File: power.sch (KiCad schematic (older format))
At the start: 50 parts, among them J10 Barrel_Jack_Switch, U6 ISL8033A, U7 TPS74401_VQFN, U8 LTC3633

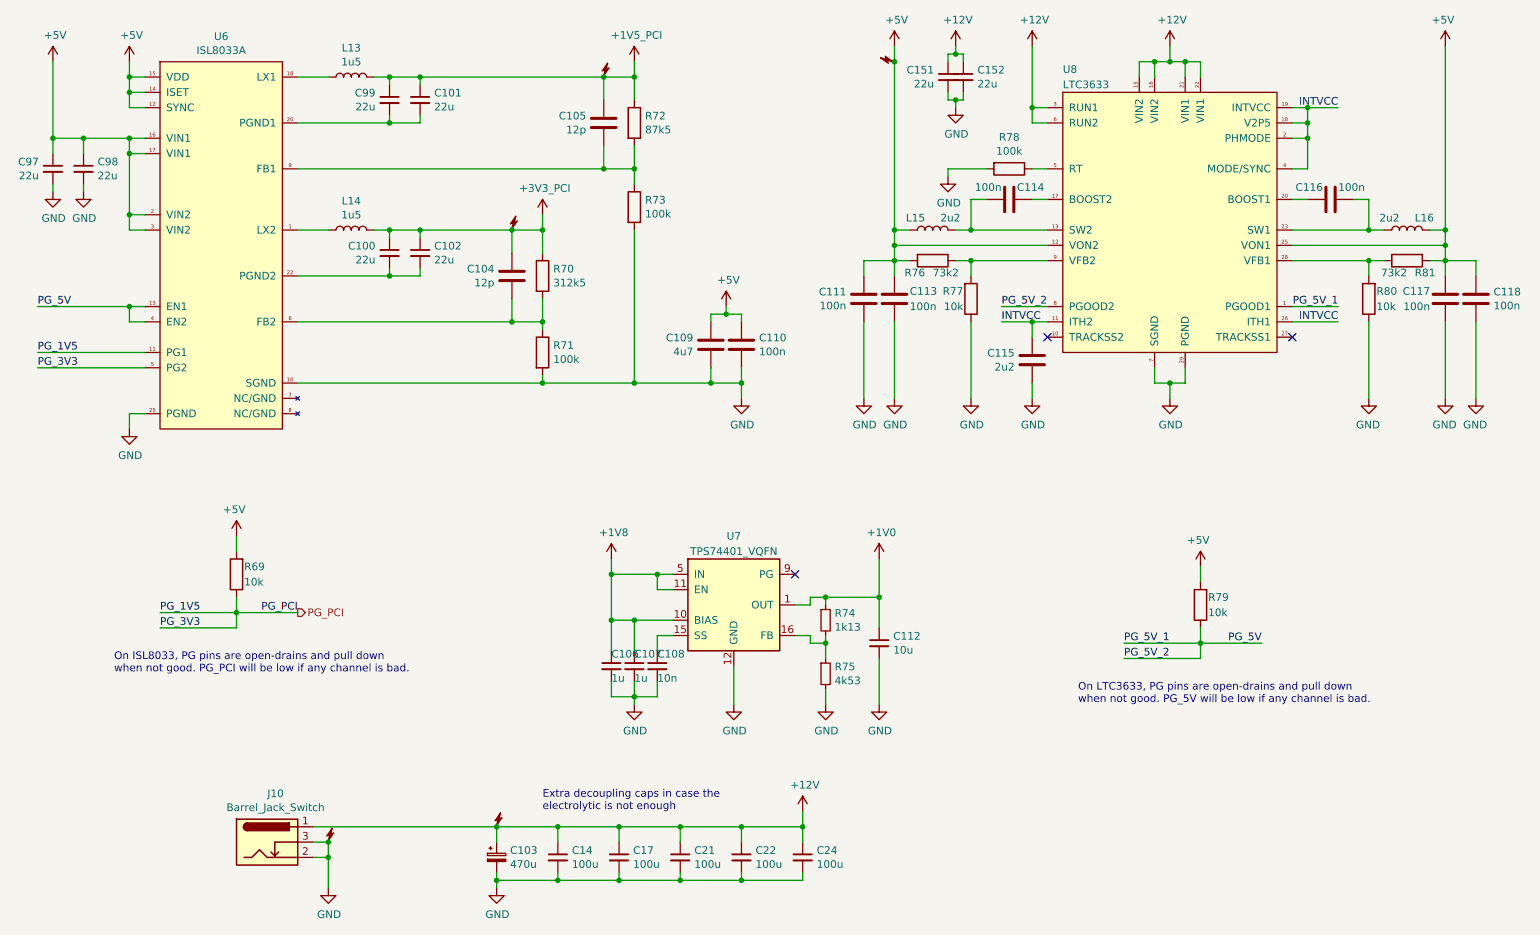
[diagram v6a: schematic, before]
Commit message: sch, pcb: Add testpads on lots of signals
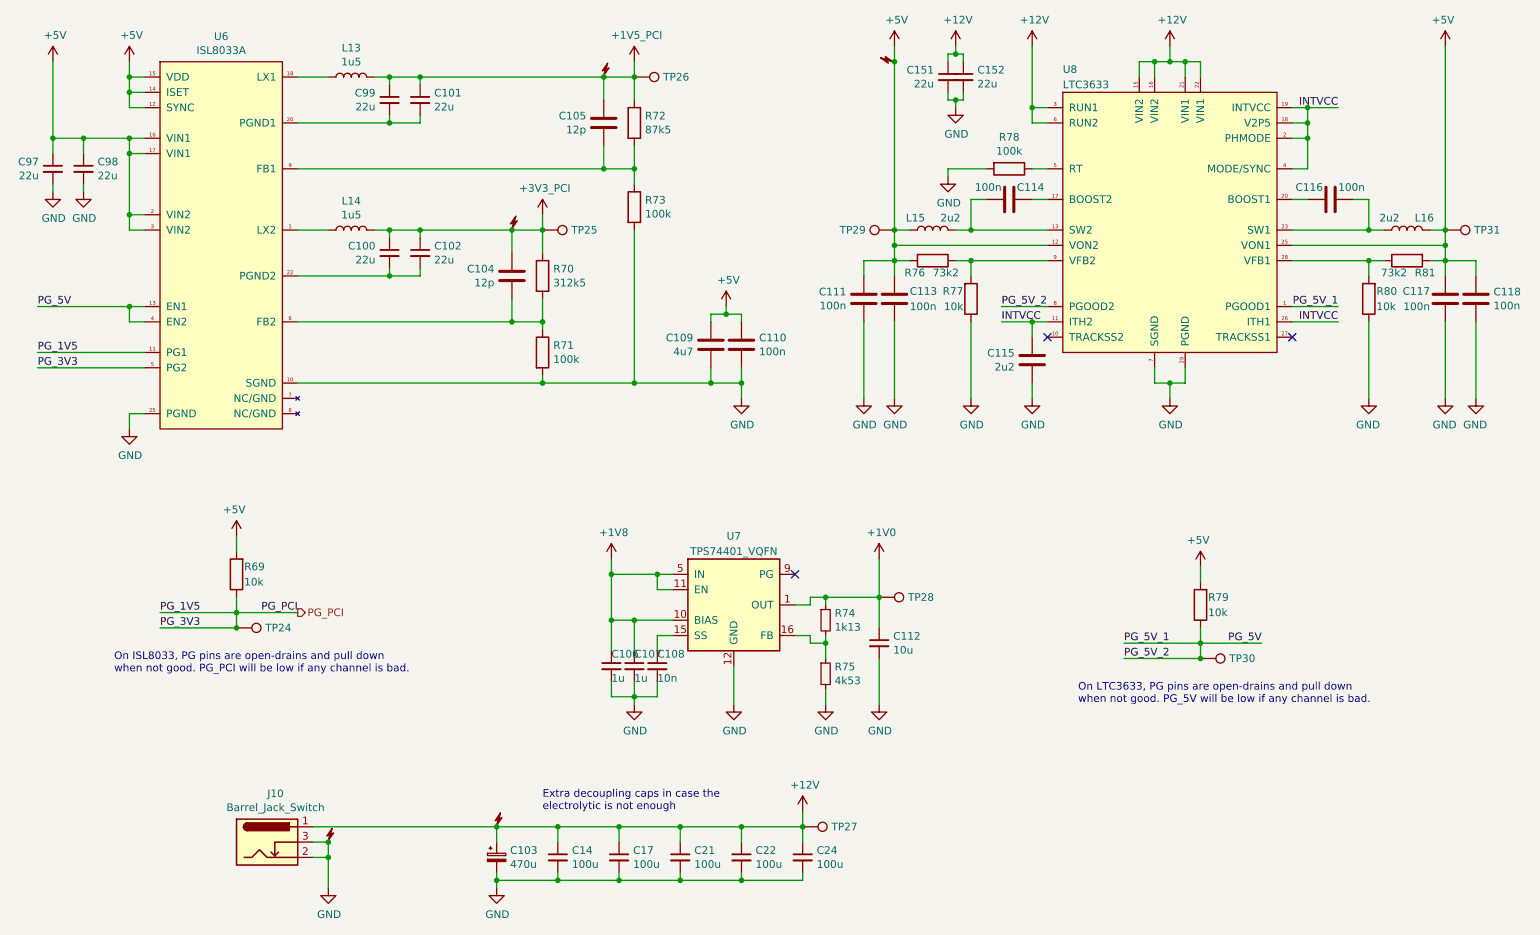
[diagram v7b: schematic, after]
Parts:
- added TP24, TP25, TP26, TP27, TP28, TP29, TP30, TP31: TestPoint, TestPoint:TestPoint_Pad_D1.0mm, symbol Connector:TestPoint
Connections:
- net +12V: now also TP27.1
- net +1V0: now also TP28.1
- net +1V5_PCI: now also TP26.1
- net +3V3_PCI: now also TP25.1
- net +5V: now also TP29.1, TP31.1
- net PG_5V: now also TP30.1
- net PG_PCI: now also TP24.1
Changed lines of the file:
@@
 Wire Wire Line
 	3000 6700 4200 6700
+$Comp
+L Connector:TestPoint TP?
+U 1 1 5D4E5684
+P 2500 5400
+AR Path="/5D05A5E1/5D4E5684" Ref="TP?"  Part="1"
+AR Path="/5CE77C37/5D4E5684" Ref="TP?"  Part="1"
+AR Path="/5D0C4621/5D4E5684" Ref="TP24"  Part="1"
+F 0 "TP24" V 2500 5588 50  0000 L CNN
+F 1 "TestPoint" V 2545 5588 50  0001 L CNN
+F 2 "TestPoint:TestPoint_Pad_D1.0mm" H 2700 5400 50  0001 C CNN
+F 3 "~" H 2700 5400 50  0001 C CNN
+	1    2500 5400
+	0    1    1    0
+$EndComp
+Connection ~ 2500 5400
+$Comp
+L Connector:TestPoint TP?
+U 1 1 5D514751
+P 8800 5600
+AR Path="/5D05A5E1/5D514751" Ref="TP?"  Part="1"
+AR Path="/5CE77C37/5D514751" Ref="TP?"  Part="1"
+AR Path="/5D0C4621/5D514751" Ref="TP30"  Part="1"
+F 0 "TP30" V 8800 5788 50  0000 L CNN
+F 1 "TestPoint" V 8845 5788 50  0001 L CNN
+F 2 "TestPoint:TestPoint_Pad_D1.0mm" H 9000 5600 50  0001 C CNN
+F 3 "~" H 9000 5600 50  0001 C CNN
+	1    8800 5600
+	0    1    1    0
+$EndComp
+Connection ~ 8800 5600
+$Comp
+L Connector:TestPoint TP?
+U 1 1 5D515165
+P 5100 1800
+AR Path="/5D05A5E1/5D515165" Ref="TP?"  Part="1"
+AR Path="/5CE77C37/5D515165" Ref="TP?"  Part="1"
+AR Path="/5D0C4621/5D515165" Ref="TP26"  Part="1"
+F 0 "TP26" V 5100 1988 50  0000 L CNN
+F 1 "TestPoint" V 5145 1988 50  0001 L CNN
+F 2 "TestPoint:TestPoint_Pad_D1.0mm" H 5300 1800 50  0001 C CNN
+F 3 "~" H 5300 1800 50  0001 C CNN
+	1    5100 1800
+	0    1    1    0
+$EndComp
+$Comp
+L Connector:TestPoint TP?
+U 1 1 5D51627F
+P 4500 2800
+AR Path="/5D05A5E1/5D51627F" Ref="TP?"  Part="1"
+AR Path="/5CE77C37/5D51627F" Ref="TP?"  Part="1"
+AR Path="/5D0C4621/5D51627F" Ref="TP25"  Part="1"
+F 0 "TP25" V 4500 2988 50  0000 L CNN
+F 1 "TestPoint" V 4545 2988 50  0001 L CNN
+F 2 "TestPoint:TestPoint_Pad_D1.0mm" H 4700 2800 50  0001 C CNN
+F 3 "~" H 4700 2800 50  0001 C CNN
+	1    4500 2800
+	0    1    1    0
+$EndComp
+$Comp
+L Connector:TestPoint TP?
+U 1 1 5D5167E4
+P 10400 2800
+AR Path="/5D05A5E1/5D5167E4" Ref="TP?"  Part="1"
+AR Path="/5CE77C37/5D5167E4" Ref="TP?"  Part="1"
+AR Path="/5D0C4621/5D5167E4" Ref="TP31"  Part="1"
+F 0 "TP31" V 10400 2988 50  0000 L CNN
+F 1 "TestPoint" V 10445 2988 50  0001 L CNN
+F 2 "TestPoint:TestPoint_Pad_D1.0mm" H 10600 2800 50  0001 C CNN
+F 3 "~" H 10600 2800 50  0001 C CNN
+	1    10400 2800
+	0    1    1    0
+$EndComp
+$Comp
+L Connector:TestPoint TP?
+U 1 1 5D5189F8
+P 6800 2800
+AR Path="/5D05A5E1/5D5189F8" Ref="TP?"  Part="1"
+AR Path="/5CE77C37/5D5189F8" Ref="TP?"  Part="1"
+AR Path="/5D0C4621/5D5189F8" Ref="TP29"  Part="1"
+F 0 "TP29" V 6800 2988 50  0000 L CNN
+F 1 "TestPoint" V 6845 2988 50  0001 L CNN
+F 2 "TestPoint:TestPoint_Pad_D1.0mm" H 7000 2800 50  0001 C CNN
+F 3 "~" H 7000 2800 50  0001 C CNN
+	1    6800 2800
+	0    -1   -1   0
+$EndComp
+$Comp
+L Connector:TestPoint TP?
+U 1 1 5D51982C
+P 6700 5200
+AR Path="/5D05A5E1/5D51982C" Ref="TP?"  Part="1"
+AR Path="/5CE77C37/5D51982C" Ref="TP?"  Part="1"
+AR Path="/5D0C4621/5D51982C" Ref="TP28"  Part="1"
+F 0 "TP28" V 6700 5388 50  0000 L CNN
+F 1 "TestPoint" V 6745 5388 50  0001 L CNN
+F 2 "TestPoint:TestPoint_Pad_D1.0mm" H 6900 5200 50  0001 C CNN
+F 3 "~" H 6900 5200 50  0001 C CNN
+	1    6700 5200
+	0    1    1    0
+$EndComp
+$Comp
+L Connector:TestPoint TP?
+U 1 1 5D51A38B
+P 6200 6700
+AR Path="/5D05A5E1/5D51A38B" Ref="TP?"  Part="1"
+AR Path="/5CE77C37/5D51A38B" Ref="TP?"  Part="1"
+AR Path="/5D0C4621/5D51A38B" Ref="TP27"  Part="1"
+F 0 "TP27" V 6200 6888 50  0000 L CNN
+F 1 "TestPoint" V 6245 6888 50  0001 L CNN
+F 2 "TestPoint:TestPoint_Pad_D1.0mm" H 6400 6700 50  0001 C CNN
+F 3 "~" H 6400 6700 50  0001 C CNN
+	1    6200 6700
+	0    1    1    0
+$EndComp
 $EndSCHEMATC

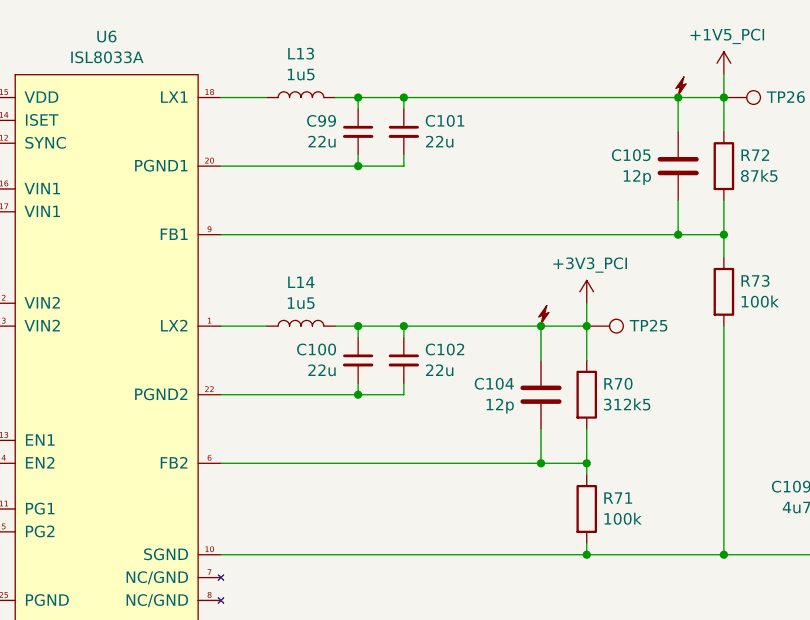
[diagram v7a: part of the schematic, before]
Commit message: sch, pcb: Connect ISL8033 PGND to GND, fix UART
Pimouss won't boot when its TXD line is pulled up, which the CH340 does.
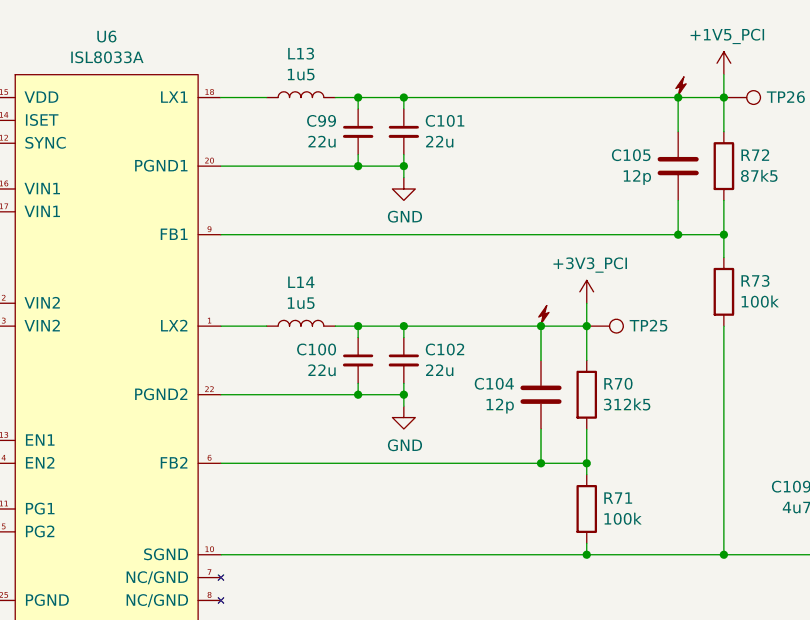
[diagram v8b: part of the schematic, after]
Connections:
- net GND: now also C100.2, C101.2, C102.2, C99.2, U6.20 (PGND1), U6.21 (PGND1), U6.22 (PGND2), U6.23 (PGND2)
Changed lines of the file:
@@
 	0    1    1    0
 $EndComp
+$Comp
+L power:GND #PWR0196
+U 1 1 5D634F9F
+P 3700 2150
+F 0 "#PWR0196" H 3700 1900 50  0001 C CNN
+F 1 "GND" H 3705 1977 50  0000 C CNN
+F 2 "" H 3700 2150 50  0001 C CNN
+F 3 "" H 3700 2150 50  0001 C CNN
+	1    3700 2150
+	1    0    0    -1
+$EndComp
+$Comp
+L power:GND #PWR0197
+U 1 1 5D635841
+P 3700 3150
+F 0 "#PWR0197" H 3700 2900 50  0001 C CNN
+F 1 "GND" H 3705 2977 50  0000 C CNN
+F 2 "" H 3700 3150 50  0001 C CNN
+F 3 "" H 3700 3150 50  0001 C CNN
+	1    3700 3150
+	1    0    0    -1
+$EndComp
+Wire Wire Line
+	3700 3150 3700 3100
+Connection ~ 3700 3100
+Wire Wire Line
+	3700 2150 3700 2100
+Connection ~ 3700 2100
 $EndSCHEMATC
